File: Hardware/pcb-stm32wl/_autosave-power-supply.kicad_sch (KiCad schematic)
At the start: 32 parts, among them J2 JST-PH, Q1 PMV32UP,215, Q3 PMV32UP,215, U11 MIC5365-3.3YD5, U12 TPS22917DBV, U8 MAX1837ETT50+T, U9 WE-TPC_5828

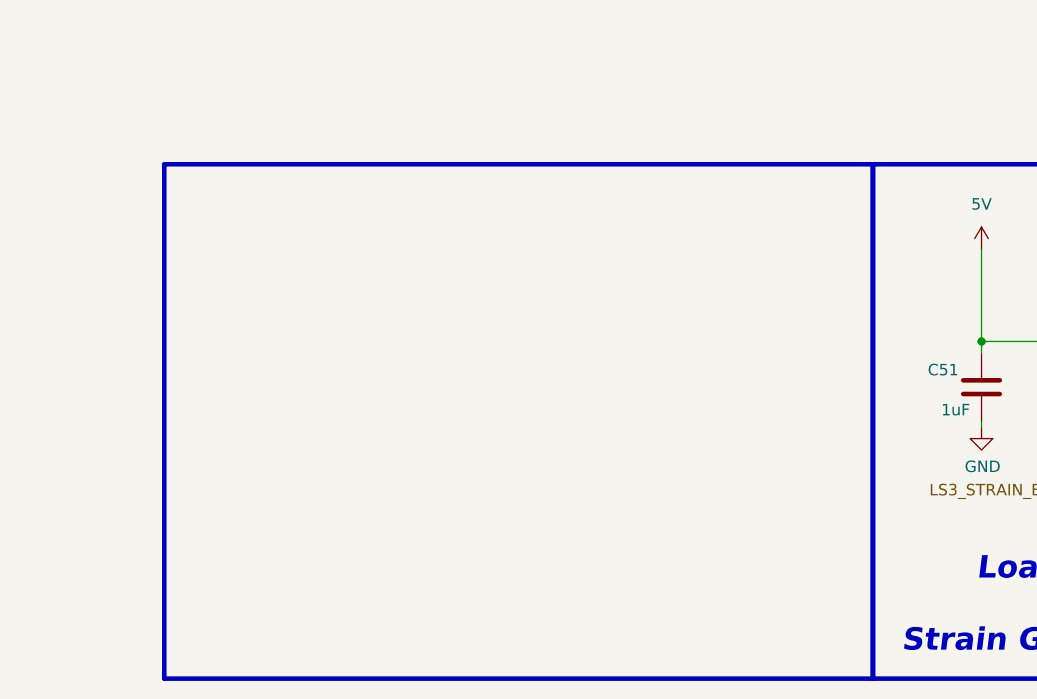
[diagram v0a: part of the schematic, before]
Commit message: rewried circuit to account ofr small details
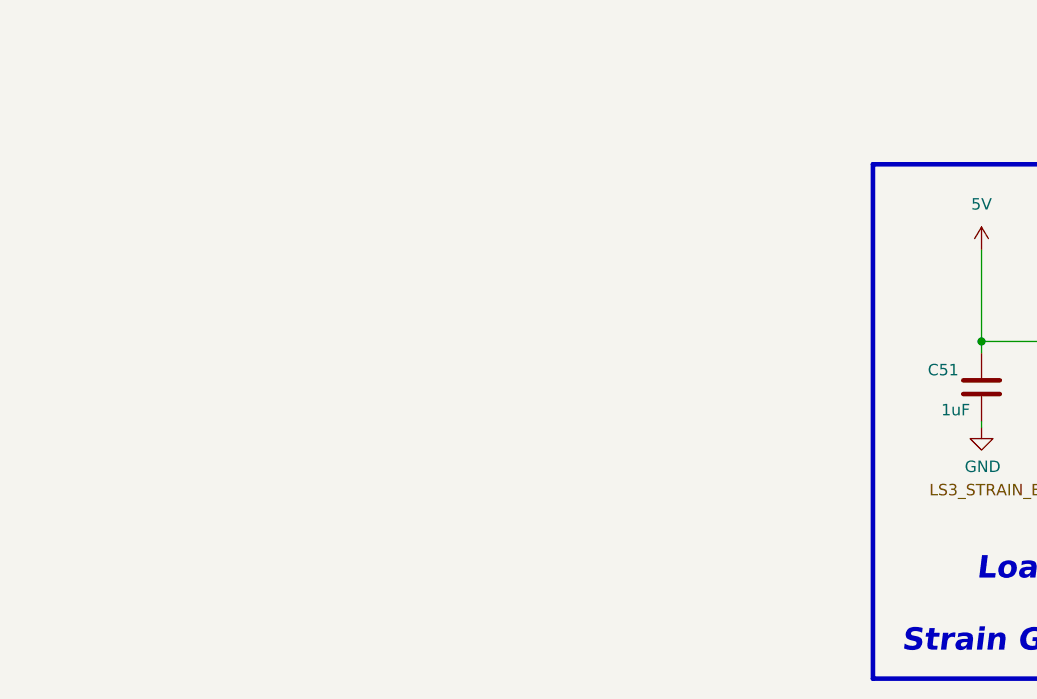
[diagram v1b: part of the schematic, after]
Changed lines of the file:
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@@
-	)
-	(rectangle
-		(start 15.875 140.335)
-		(end 94.615 197.485)
-		(stroke
-			(width 0.508)
-			(type default)
-		)
-		(fill
-			(type none)
-		)
 	)
 	(rectangle
